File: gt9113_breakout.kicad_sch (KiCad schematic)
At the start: 9 parts, among them J6 504740-5100, J7 504740-5100, U9 GT9113

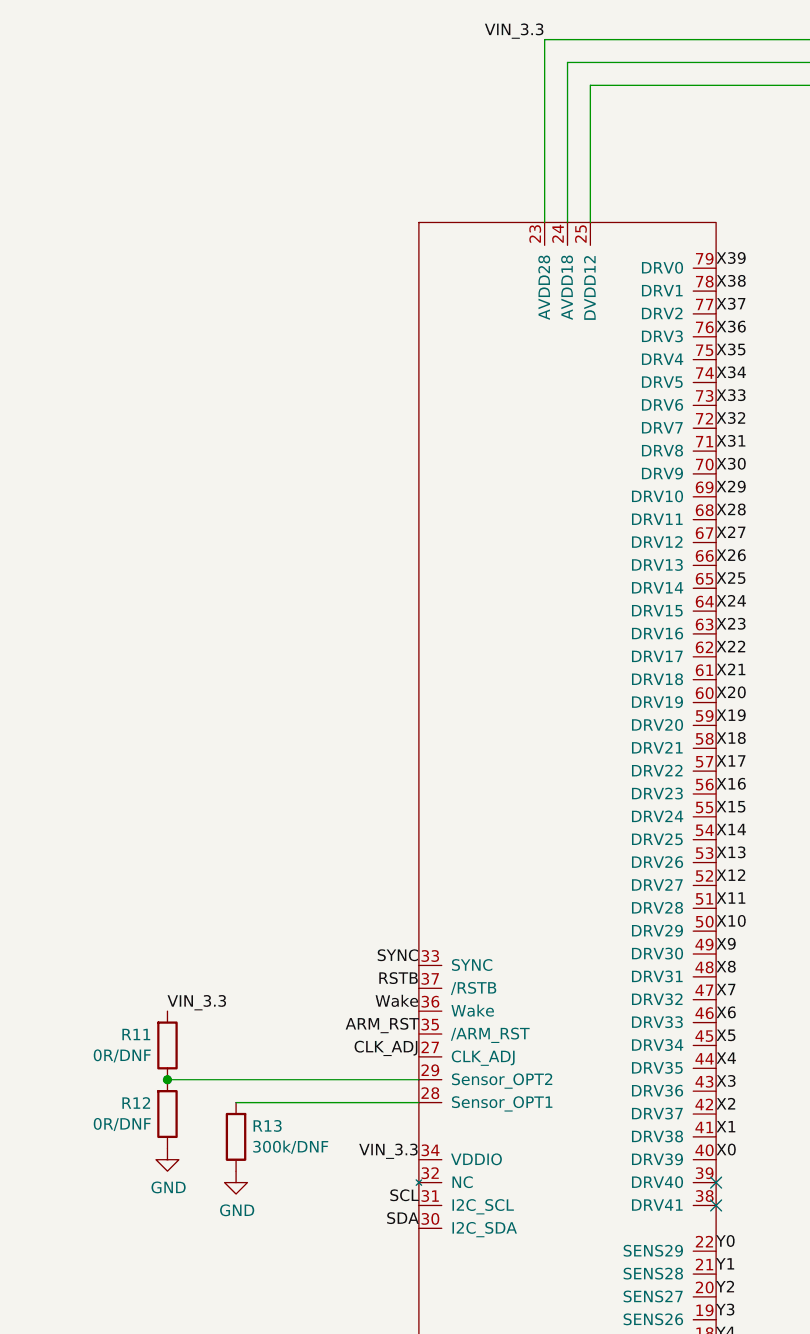
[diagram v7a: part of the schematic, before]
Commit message: Lots of changes: add USB switch in charger circuit, reroute differential pairs using proper track widths; make CM4 courtyard the full size. Fixes #11.
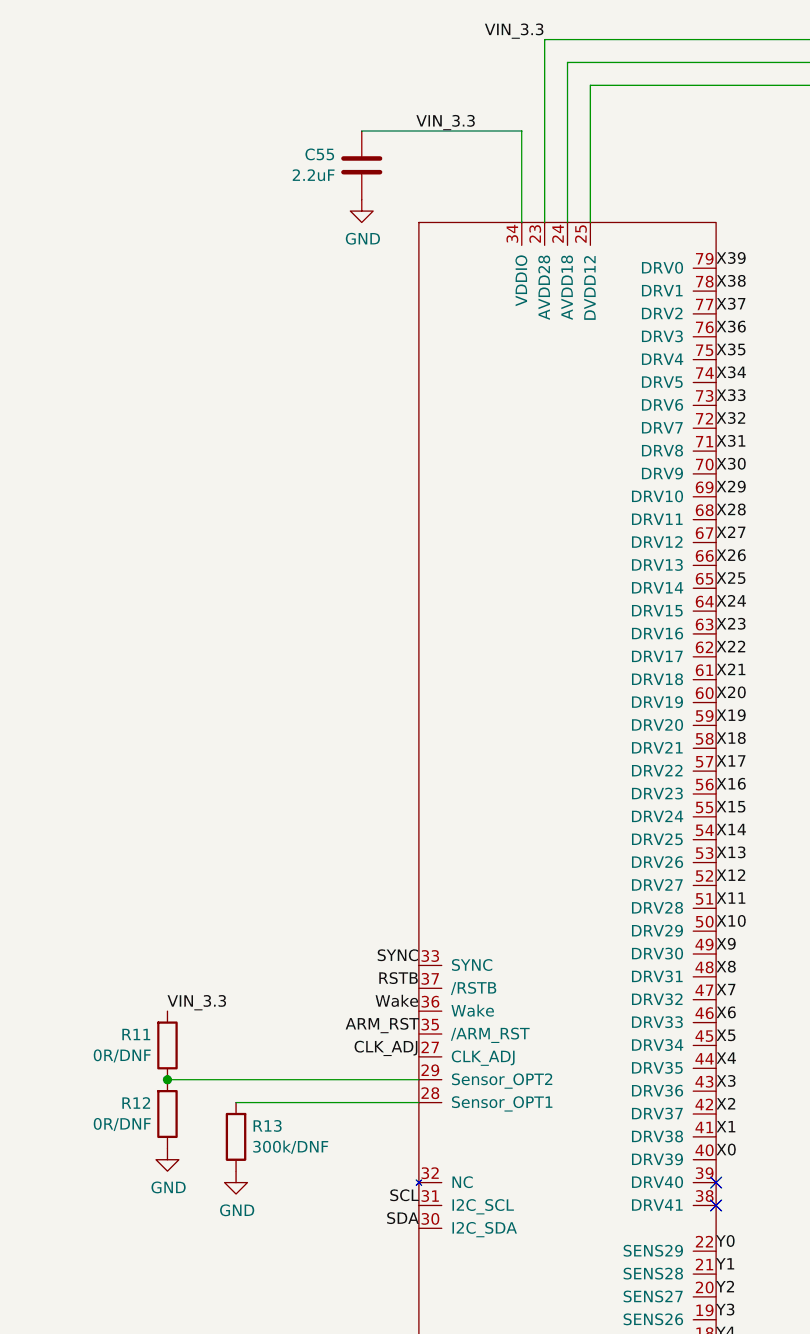
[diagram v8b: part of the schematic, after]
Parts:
- added C55: 2.2uF, Capacitor_SMD:C_0402_1005Metric, symbol Device:C
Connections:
- net GND: now also C55.2
- net VIN_3.3: now also C55.1
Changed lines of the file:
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@@
+    (stroke (width 0) (type solid) (color 0 0 0 0))
+  )
+  (wire (pts (xy 227.33 34.29) (xy 245.11 34.29))
     (stroke (width 0) (type solid) (color 0 0 0 0))
   )
@@
     (stroke (width 0) (type solid) (color 0 0 0 0))
   )
+  (wire (pts (xy 245.11 34.29) (xy 245.11 44.45))
+    (stroke (width 0) (type solid) (color 0 0 0 0))
+  )
   (wire (pts (xy 247.65 24.13) (xy 306.07 24.13))
     (stroke (width 0) (type solid) (color 0 0 0 0))
@@
     (effects (font (size 1.27 1.27)) (justify right bottom))
   )
-  (label "VIN_3.3" (at 233.68 148.59 180)
-    (effects (font (size 1.27 1.27)) (justify right bottom))
-  )
   (label "SCL" (at 233.68 153.67 180)
     (effects (font (size 1.27 1.27)) (justify right bottom))
   )
   (label "SDA" (at 233.68 156.21 180)
+    (effects (font (size 1.27 1.27)) (justify right bottom))
+  )
+  (label "VIN_3.3" (at 240.03 34.29 180)
     (effects (font (size 1.27 1.27)) (justify right bottom))
   )
@@
     (pin "1")
   )
+  (symbol (lib_id "power:GND") (at 227.33 41.91 0) (unit 1)
+    (in_bom yes) (on_board yes)
+    (property "Reference" "#PWR01" (id 0) (at 227.33 48.26 0)
+      (effects (font (size 1.27 1.27)) hide)
+    )
+    (property "Value" "GND" (id 1) (at 227.457 46.3042 0))
+    (property "Footprint" "" (id 2) (at 227.33 41.91 0)
+      (effects (font (size 1.27 1.27)) hide)
+    )
+    (property "Datasheet" "" (id 3) (at 227.33 41.91 0)
+      (effects (font (size 1.27 1.27)) hide)
+    )
+    (pin "1")
+  )
   (symbol (lib_id "power:GND") (at 247.65 237.49 0) (unit 1)
     (in_bom yes) (on_board yes)
@@
       (effects (font (size 1.27 1.27)) hide)
     )
+    (pin "1")
+    (pin "2")
+  )
+  (symbol (lib_id "Device:C") (at 227.33 38.1 0) (mirror y) (unit 1)
+    (in_bom yes) (on_board yes)
+    (property "Reference" "C55" (id 0) (at 224.409 36.9316 0)
+      (effects (font (size 1.27 1.27)) (justify left))
+    )
+    (property "Value" "2.2uF" (id 1) (at 224.409 39.243 0)
+      (effects (font (size 1.27 1.27)) (justify left))
+    )
+    (property "Footprint" "Capacitor_SMD:C_0402_1005Metric" (id 2) (at 226.3648 41.91 0)
+      (effects (font (size 1.27 1.27)) hide)
+    )
+    (property "Datasheet" "~" (id 3) (at 227.33 38.1 0)
+      (effects (font (size 1.27 1.27)) hide)
+    )
